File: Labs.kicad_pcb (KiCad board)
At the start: 2 copper layers, 46.5 x 34.8 mm, 29 parts, among them J1 Conn_02x05_Counter_Clockwise, SW1BOOT1 SW_Push, SW2NRST1 SW_Push, U1 STM32F407VGTx, Y1 Crystal

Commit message: feat: add tracing
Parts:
- removed U1: STM32F407VGTx, Package_QFP:LQFP-100_14x14mm_P0.5mm
- added I2C: Conn_01x02_Pin, Connector_PinHeader_2.54mm:PinHeader_1x02_P2.54mm_Horizontal, F.Cu at (131.2, 78.9)
- added LQFP100: STM32F407VGTx, Package_QFP:LQFP-100_14x14mm_P0.5mm, F.Cu at (146.8, 92.0)
- added R8: R 2.2 kOhm, Resistor_SMD:R_0805_2012Metric_Pad1.20x1.40mm_HandSolder, B.Cu at (139.5, 82.5)
- added R9: R 2.2 kOhm, Resistor_SMD:R_0805_2012Metric_Pad1.20x1.40mm_HandSolder, B.Cu at (136.2, 82.5)
- added SPI: Conn_01x04_Pin, Connector_PinHeader_2.54mm:PinHeader_1x04_P2.54mm_Horizontal, F.Cu at (146.2, 78.9)
- added UART: Conn_01x02_Pin, Connector_PinHeader_2.54mm:PinHeader_1x02_P2.54mm_Horizontal, F.Cu at (138.7, 78.9)
- C6: moved to B.Cu
- J1: value Conn_02x05_Counter_Clockwise -> PROG_port
- Y1: moved to F.Cu
- moved J1 38.8 mm to (157.7, 80.8)
- moved RV1 34.7 mm to (162.4, 97.7), turned to 180 degrees
- moved RV2 21.1 mm to (162.5, 105.8), turned to 180 degrees
- moved User1 19.5 mm to (140.8, 104.0), turned to 0 degrees
- moved C1 18.1 mm to (144.5, 88.5), turned to 180 degrees
- moved SW2NRST1 16.6 mm to (127.5, 94.0)
- moved C6 15.7 mm to (130.7, 96.3), turned to 180 degrees
- moved R6 15.3 mm to (144.0, 106.2), turned to 180 degrees
- moved C2 13.8 mm to (144.5, 92.0), turned to 180 degrees
- moved C7 13.5 mm to (149.3, 88.5), turned to 0 degrees
- moved SW1BOOT1 10.3 mm to (127.5, 84.0)
- moved C3 9.62 mm to (144.5, 95.5), turned to 180 degrees
- moved C8 9.52 mm to (149.3, 92.0), turned to 0 degrees
- moved C5 9.00 mm to (135.0, 103.7)
- moved C4 8.14 mm to (135.0, 108.2)
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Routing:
- net +3.3V: track 162.2 -> 133.6 mm, vias 1 -> 6
- net /I2C_SDA: track 0.00 -> 21.9 mm
- net /I2C_SCL: track 0.00 -> 21.8 mm
- net GND: track 22.9 -> 7.49 mm, vias 9 -> 5
- net /UART_RX: track 0.00 -> 11.4 mm
- net /UART_TX: track 0.00 -> 11.3 mm
- net /UButton_2: track 16.0 -> 25.9 mm
- net /EXTAL: track 17.3 -> 26.9 mm, vias 1 -> 2
- net /XTAL: track 10.1 -> 19.2 mm
- net /SPI_SCK: track 0.00 -> 8.25 mm
- net /SPI_MOSI: track 0.00 -> 8.20 mm
- net /SPI_MISO: track 0.00 -> 8.15 mm
- net /NRST: track 34.3 -> 41.9 mm
- net /ADC_1: track 22.0 -> 28.6 mm, vias 1 -> 2
- net /SPI_NSS: track 0.00 -> 6.06 mm
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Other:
- board size 46.5 x 34.8 mm -> 44.8 x 36.2 mm

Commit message: fix: minor fixes
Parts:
- removed I2C, UART: Conn_01x02_Pin, Connector_PinHeader_2.54mm:PinHeader_1x02_P2.54mm_Horizontal
- added J2: Conn_01x03_Pin, Connector_PinHeader_2.54mm:PinHeader_1x03_P2.54mm_Horizontal, F.Cu at (137.8, 78.9)
- added J3: Conn_01x04_Pin, Connector_PinHeader_2.54mm:PinHeader_1x04_P2.54mm_Horizontal, F.Cu at (126.6, 78.9)
- moved J4 0.27 mm to (146.5, 78.9)
- renumbered User1 to Button_1, User2 to Button_2, C6 to C1, C9 to C2, C5 to C3, C8 to C4, C4 to C5, C7 to C6, C3 to C7, C2 to C8, C1 to C9, SPI to J4, R8 to R2, R9 to R3, R2 to R4, R4 to R6, R3 to R7, R6 to R8, R7 to R9, LQFP100 to U1
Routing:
- net +3.3V: track 133.6 -> 144.7 mm
- net /I2C_SCL: track 21.8 -> 27.4 mm
- net /I2C_SDA: track 21.9 -> 26.9 mm
- net /UART_RX: track 11.4 -> 9.82 mm
- net /UART_TX: track 11.3 -> 9.82 mm
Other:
- board size 44.8 x 36.2 mm -> 45.2 x 36.2 mm

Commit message: fix: silkscreen
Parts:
- renumbered J3 to I2C, J4 to SPI, J2 to UART
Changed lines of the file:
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@@
 		(descr "Through hole angled pin header, 1x04, 2.54mm pitch, 6mm pin length, single row")
 		(tags "Through hole angled pin header THT 1x04 2.54mm single row")
-		(property "Reference" "J4"
-			(at -2.115 -0.73 0)
+		(property "Reference" "SPI"
+			(at -1.615 1.52 0)
 			(layer "F.SilkS")
 			(effects
@@
 		(descr "Through hole angled pin header, 1x04, 2.54mm pitch, 6mm pin length, single row")
 		(tags "Through hole angled pin header THT 1x04 2.54mm single row")
-		(property "Reference" "J3"
-			(at -2.1 -0.88 180)
+		(property "Reference" "I2C"
+			(at -1.6 1.37 180)
 			(layer "F.SilkS")
 			(effects
@@
 		(descr "Through hole angled pin header, 1x03, 2.54mm pitch, 6mm pin length, single row")
 		(tags "Through hole angled pin header THT 1x03 2.54mm single row")
-		(property "Reference" "J2"
-			(at -2.1 -0.82 180)
+		(property "Reference" "UART"
+			(at -1.6 1.93 180)
 			(layer "F.SilkS")
 			(effects

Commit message: fix: minor fixes
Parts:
- renumbered I2C to I2C1, SPI to SPI1, UART to UART1
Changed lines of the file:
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@@
 		(descr "Through hole angled pin header, 1x04, 2.54mm pitch, 6mm pin length, single row")
 		(tags "Through hole angled pin header THT 1x04 2.54mm single row")
-		(property "Reference" "SPI"
-			(at -1.615 1.52 0)
+		(property "Reference" "SPI1"
+			(at -1.615 1.77 0)
 			(layer "F.SilkS")
 			(effects
@@
 		(descr "Through hole angled pin header, 1x04, 2.54mm pitch, 6mm pin length, single row")
 		(tags "Through hole angled pin header THT 1x04 2.54mm single row")
-		(property "Reference" "I2C"
-			(at -1.6 1.37 180)
+		(property "Reference" "I2C1"
+			(at -1.6 1.87 180)
 			(layer "F.SilkS")
 			(effects
@@
 		(descr "Through hole angled pin header, 1x03, 2.54mm pitch, 6mm pin length, single row")
 		(tags "Through hole angled pin header THT 1x03 2.54mm single row")
-		(property "Reference" "UART"
-			(at -1.6 1.93 180)
+		(property "Reference" "UART1"
+			(at -1.6 2.43 180)
 			(layer "F.SilkS")
 			(effects

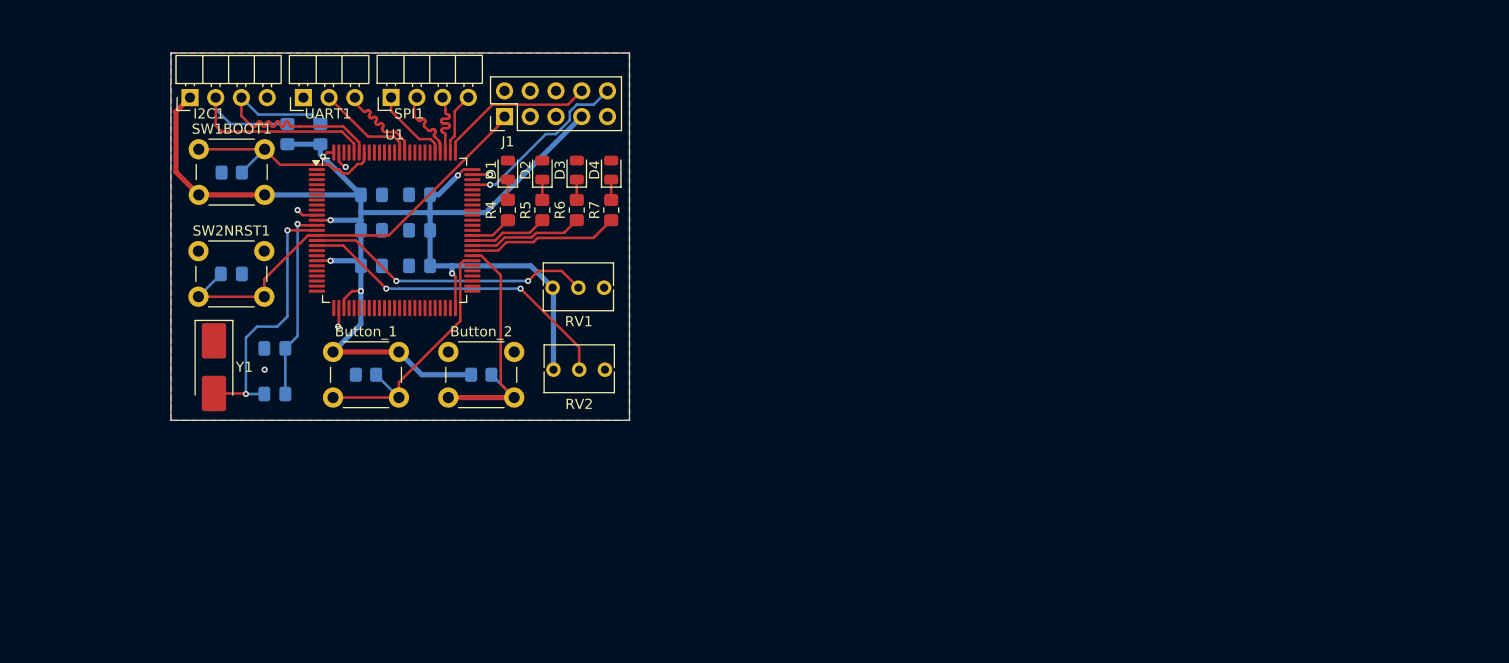
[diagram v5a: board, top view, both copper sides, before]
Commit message: feat: add pwr supply from type-c connector
feat: add pwr supply from bat

feat: add dc/dc lower pwr

feat: add pwr for extern sensors

fix: replace adc to another pin
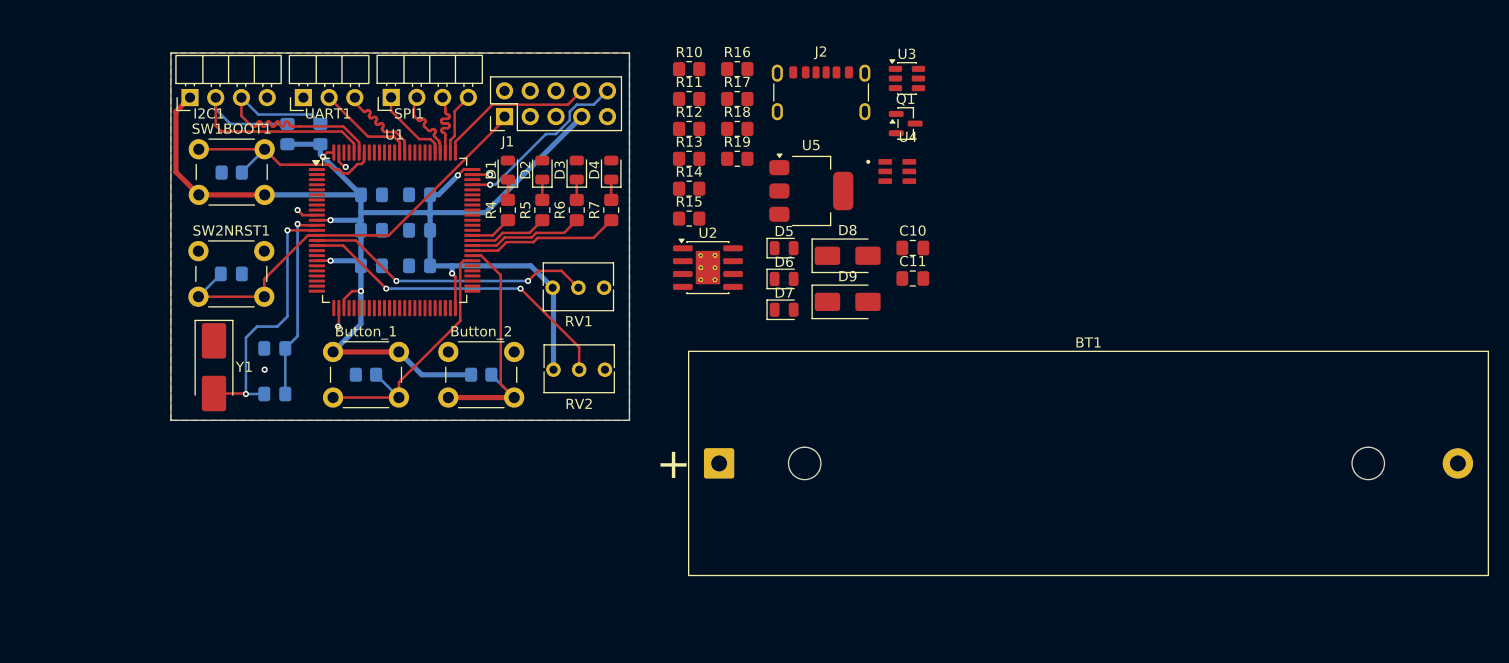
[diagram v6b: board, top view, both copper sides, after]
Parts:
- added BT1: Battery_Cell, Battery:BatteryHolder_MPD_BH-18650-PC, F.Cu at (178.8, 115.0)
- added C10: C 10 uF, Capacitor_SMD:C_0805_2012Metric_Pad1.18x1.45mm_HandSolder, F.Cu at (198.0, 93.7)
- added C11: C 100 uF, Capacitor_SMD:C_0805_2012Metric_Pad1.18x1.45mm_HandSolder, F.Cu at (198.0, 96.8)
- added D5: LED Green, LED_SMD:LED_0805_2012Metric, F.Cu at (185.3, 93.8)
- added D6: LED Blue, LED_SMD:LED_0805_2012Metric, F.Cu at (185.3, 96.8)
- added D7: LED Red, LED_SMD:LED_0805_2012Metric, F.Cu at (185.3, 99.8)
- added D8: SS34, Diode_SMD:D_SMA, F.Cu at (191.5, 94.5)
- added D9: SS34, Diode_SMD:D_SMA, F.Cu at (191.5, 99.1)
- added J2: USB_C_Receptacle_PowerOnly_6P, Connector_USB:USB_C_Receptacle_GCT_USB4125-xx-x-0190_6P_TopMnt_Horizontal, F.Cu at (188.9, 79.5)
- added Q1: AO3401A, Package_TO_SOT_SMD:SOT-23, F.Cu at (197.3, 81.5)
- added R10: R 5.1 kOhm, Resistor_SMD:R_0805_2012Metric_Pad1.20x1.40mm_HandSolder, F.Cu at (175.9, 76.1)
- added R11: R 5.1 kOhm, Resistor_SMD:R_0805_2012Metric_Pad1.20x1.40mm_HandSolder, F.Cu at (175.9, 79.0)
- added R12: R 1 kOhm, Resistor_SMD:R_0805_2012Metric_Pad1.20x1.40mm_HandSolder, F.Cu at (175.9, 82.0)
- added R13: R 1 kOhm, Resistor_SMD:R_0805_2012Metric_Pad1.20x1.40mm_HandSolder, F.Cu at (175.9, 84.9)
- added R14: R 0 Ohm, Resistor_SMD:R_0805_2012Metric_Pad1.20x1.40mm_HandSolder, F.Cu at (175.9, 87.9)
- added R15: R 1.5 kOhm, Resistor_SMD:R_0805_2012Metric_Pad1.20x1.40mm_HandSolder, F.Cu at (175.9, 90.8)
- added R16: R 1 kOhm, Resistor_SMD:R_0805_2012Metric_Pad1.20x1.40mm_HandSolder, F.Cu at (180.6, 76.1)
- added R17: R 100 Ohm, Resistor_SMD:R_0805_2012Metric_Pad1.20x1.40mm_HandSolder, F.Cu at (180.6, 79.0)
- added R18: R 10 kOhm, Resistor_SMD:R_0805_2012Metric_Pad1.20x1.40mm_HandSolder, F.Cu at (180.6, 82.0)
- added R19: R 1 kOhm, Resistor_SMD:R_0805_2012Metric_Pad1.20x1.40mm_HandSolder, F.Cu at (180.6, 84.9)
- added U2: TP4056-42-ESOP8, Package_SO:SOIC-8-1EP_3.9x4.9mm_P1.27mm_EP2.41x3.3mm_ThermalVias, F.Cu at (177.7, 95.7)
- added U3: DW01A, Package_TO_SOT_SMD:SOT-23-6, F.Cu at (197.4, 77.0)
- added U4: 8205A, 8205A:SOT95P285X140-6N, F.Cu at (196.4, 86.2)
- added U5: AMS1117-3.3, Package_TO_SOT_SMD:SOT-223-3_TabPin2, F.Cu at (187.9, 88.1)
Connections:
- J1 pad 7: +3.3V -> unconnected-(J1-Pin_7-Pad7)

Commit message: feat: add tracing
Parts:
- added C13: C 10 uF, Capacitor_SMD:C_0805_2012Metric_Pad1.18x1.45mm_HandSolder, F.Cu at (158.2, 87.6)
- added C14: C 10 uF, Capacitor_SMD:C_0805_2012Metric_Pad1.18x1.45mm_HandSolder, B.Cu at (134.6, 89.4)
- added GND1: Conn_01x04_Pin, Connector_PinHeader_2.54mm:PinHeader_1x04_P2.54mm_Horizontal, F.Cu at (161.7, 75.5)
- added PWR1: Conn_01x04_Pin, Connector_PinHeader_2.54mm:PinHeader_1x04_P2.54mm_Horizontal, F.Cu at (175.0, 75.5)
- D5: value LED Green -> STANDBY
- D6: value LED Blue -> CHARGE
- D7: value LED Red -> BAT
- moved C10 39.9 mm to (158.3, 98.3)
- moved U3 32.7 mm to (177.1, 102.7)
- moved U4 29.2 mm to (172.4, 102.7)
- moved R16 28.5 mm to (181.6, 104.6), turned to 180 degrees
- moved U5 28.2 mm to (160.3, 82.7)
- moved R17 24.0 mm to (185.0, 102.7), turned to 180 degrees
- moved C2 23.1 mm to (130.2, 82.5), turned to 180 degrees
- moved C3 20.5 mm to (119.1, 90.6)
- moved C5 20.5 mm to (119.1, 95.1)
- moved Y1 20.5 mm to (113.1, 92.5)
- moved C4 20.1 mm to (130.2, 86.0), turned to 180 degrees
- moved R14 19.5 mm to (158.3, 96.2)
- moved D9 19.4 mm to (173.8, 91.2), turned to 180 degrees
- moved C6 19.2 mm to (130.2, 89.4), turned to 180 degrees
- moved R15 18.4 mm to (163.6, 104.4), turned to 180 degrees
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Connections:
- C11 pad 1: Net-(U3-GND) -> Net-(BT1--)
- R17 pad 1: Net-(U2-BAT) -> +BATT
- U1 pad 15: /ADC_1 -> unconnected-(U1-PC0-Pad15)
- U1 pad 16: /ADC_2 -> unconnected-(U1-PC1-Pad16)
- U1 pad 33: unconnected-(U1-PC4-Pad33) -> /ADC_1
- U1 pad 34: unconnected-(U1-PC5-Pad34) -> /ADC_2
- U2 pad 5: Net-(U2-BAT) -> +BATT
- U3 pad 6: Net-(U3-GND) -> Net-(BT1--)
- U4 pad 2: Net-(U4-Pad2) -> unconnected-(U4-Pad2)
- U4 pad 5: Net-(U4-Pad2) -> unconnected-(U4-Pad2)_1
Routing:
- net VBUS: track 0.00 -> 87.4 mm
- net Net-(BT1--): track 0.00 -> 86.7 mm
- net Net-(D8-K): track 0.00 -> 76.7 mm
- net +BATT: track 0.00 -> 43.1 mm
- net +3.3V: track 144.7 -> 183.8 mm
- net Net-(U2-~{CHRG}): track 0.00 -> 27.7 mm
- net Net-(BT1-+): track 0.00 -> 25.6 mm
- net Net-(U2-~{STDBY}): track 0.00 -> 21.5 mm
- net GND: track 7.49 -> 22.9 mm, vias 5 -> 11
- net /EXTAL: track 26.9 -> 16.1 mm, vias 2 -> 1
- net /NRST: track 41.9 -> 52.1 mm
- net Net-(Q1-G): track 0.00 -> 9.52 mm
- net /XTAL: track 19.2 -> 10.2 mm
- net /ADC_2: track 32.3 -> 26.1 mm
- net Net-(U3-CS): track 0.00 -> 5.98 mm
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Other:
- board size 45.2 x 36.2 mm -> 85.2 x 61.3 mm
